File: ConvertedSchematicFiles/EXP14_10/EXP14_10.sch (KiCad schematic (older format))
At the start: 14 parts, among them U1 uA741

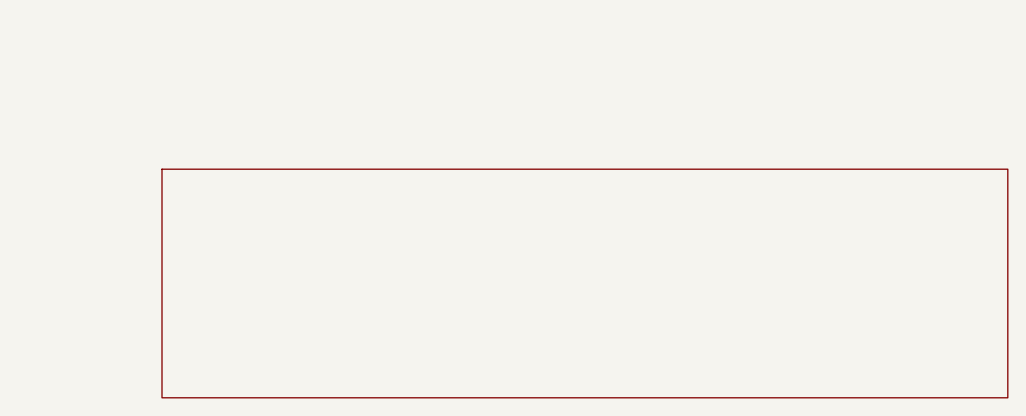
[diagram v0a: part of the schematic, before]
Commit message: Excluded some components. These no longer appear after conversion. When calling shell commands, filenames are in "quotes"
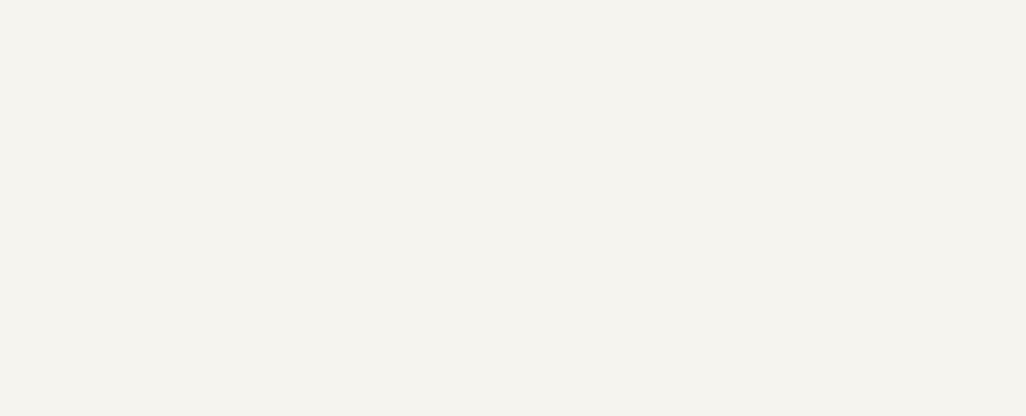
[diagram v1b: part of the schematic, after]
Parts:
- removed titleblk: titleblk, symbol TITLEBLK_PSPICE
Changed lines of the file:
@@
 	0    -1    1    0
-$EndComp
-$Comp
-L TITLEBLK_PSPICE titleblk
-U 1 1 32520059
-P 9700 7200
-F 0 "titleblk" H 19400 14400 30  0001 L CNN
-F 1 "titleblk" H 19400 14480 30  0001 L CNN
-	1    9700 7200
-	1    0    0    1
 $EndComp
 Wire Wire Line

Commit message: Ports issue fixed. Now annotation for ports is #PWR? function added "itos"
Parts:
- removed EGND: EGND, symbol EGND_PSPICE
- removed GND_EARTH (x4): GND_EARTH, symbol GND_EARTH_PSPICE
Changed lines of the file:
@@
 $EndDescr
 $Comp
-L GND_EARTH_PSPICE GND_EARTH
+L GND_EARTH_PSPICE #PWR1
 U 1 1 14289383
 P 2500 3400
-F 0 "GND_EARTH" H 5000 6800 30  0001 L CNN
+F 0 "#PWR1" H 5000 6800 30  0001 L CNN
 F 1 "GND_EARTH" H 5000 6880 30  0001 L CNN
 	1    2500 3400
@@
 $EndComp
 $Comp
-L GND_EARTH_PSPICE GND_EARTH
+L GND_EARTH_PSPICE #PWR2
 U 1 1 46930886
 P 2200 4600
-F 0 "GND_EARTH" H 4400 9200 30  0001 L CNN
+F 0 "#PWR2" H 4400 9200 30  0001 L CNN
 F 1 "GND_EARTH" H 4400 9280 30  0001 L CNN
 	1    2200 4600
@@
 $EndComp
 $Comp
-L GND_EARTH_PSPICE GND_EARTH
+L GND_EARTH_PSPICE #PWR3
 U 1 1 71692777
 P 1400 3700
-F 0 "GND_EARTH" H 2800 7400 30  0001 L CNN
+F 0 "#PWR3" H 2800 7400 30  0001 L CNN
 F 1 "GND_EARTH" H 2800 7480 30  0001 L CNN
 	1    1400 3700
@@
 $EndComp
 $Comp
-L GND_EARTH_PSPICE GND_EARTH
+L GND_EARTH_PSPICE #PWR4
 U 1 1 14636915
 P 900 4500
-F 0 "GND_EARTH" H 1800 9000 30  0001 L CNN
+F 0 "#PWR4" H 1800 9000 30  0001 L CNN
 F 1 "GND_EARTH" H 1800 9080 30  0001 L CNN
 	1    900 4500
@@
 $EndComp
 $Comp
-L EGND_PSPICE EGND
+L EGND_PSPICE #PWR5
 U 1 1 77747793
 P 3100 4400
-F 0 "EGND" H 6200 8800 30  0001 L CNN
+F 0 "#PWR5" H 6200 8800 30  0001 L CNN
 F 1 "EGND" H 6200 8880 30  0001 L CNN
 	1    3100 4400

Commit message: Added LICENSE.txt
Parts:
- VIN: value VAC -> AC
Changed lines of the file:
@@
 $EndDescr
 $Comp
-L GND_EARTH_PSPICE #PWR1
+L GND #PWR1
 U 1 1 14289383
 P 2500 3400
@@
 $EndComp
 $Comp
-L GND_EARTH_PSPICE #PWR2
+L GND #PWR2
 U 1 1 46930886
 P 2200 4600
@@
 $EndComp
 $Comp
-L GND_EARTH_PSPICE #PWR3
+L GND #PWR3
 U 1 1 71692777
 P 1400 3700
@@
 $EndComp
 $Comp
-L GND_EARTH_PSPICE #PWR4
+L GND #PWR4
 U 1 1 14636915
 P 900 4500
@@
 $EndComp
 $Comp
-L EGND_PSPICE #PWR5
+L GND #PWR5
 U 1 1 77747793
 P 3100 4400
@@
 P 900 4100
 F 0 "VIN" H 900 4100 30  0000 L CNN
-F 1 "VAC" H 900 4180 30  0000 L CNN
+F 1 "AC" H 900 4180 30  0000 L CNN
 	1    900 4100
 	1    0    0    1

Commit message: Orientation fix. Library components are now inverted, with +ve y axis going up. In Schematic files, +ve y axis is downwards. This is how the KiCad libraries are. As a result of the above fixed, the converted GND is now oriented correctly.
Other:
- moved on the sheet: VIN
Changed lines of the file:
@@
 F 1 "GND_EARTH" H 5000 6880 30  0001 L CNN
 	1    2500 3400
-	1    0    0    1
+	1    0    0    -1
 $EndComp
 $Comp
@@
 F 1 "GND_EARTH" H 4400 9280 30  0001 L CNN
 	1    2200 4600
-	1    0    0    1
+	1    0    0    -1
 $EndComp
 $Comp
@@
 F 1 "GND_EARTH" H 2800 7480 30  0001 L CNN
 	1    1400 3700
-	1    0    0    1
+	1    0    0    -1
 $EndComp
 $Comp
@@
 F 1 "GND_EARTH" H 1800 9080 30  0001 L CNN
 	1    900 4500
-	1    0    0    1
+	1    0    0    -1
 $EndComp
 $Comp
@@
 F 1 "EGND" H 6200 8880 30  0001 L CNN
 	1    3100 4400
-	1    0    0    1
+	1    0    0    -1
 $EndComp
 $Comp
@@
 F 1 "15v" H 2200 3870 30  0000 C CNN
 	1    2200 3600
-	-1    0    0    -1
+	-1    0    0    1
 $EndComp
 $Comp
@@
 F 1 "15v" H 2200 4490 30  0000 C CNN
 	1    2200 4600
-	-1    0    0    -1
+	-1    0    0    1
 $EndComp
 $Comp
@@
 F 1 "R" H 1400 3780 30  0001 L CNN
 	1    1400 3700
-	1    0    0    1
+	1    0    0    -1
 $EndComp
 $Comp
@@
 F 1 "10k" H 2400 4950 30  0000 L CNN
 	1    2400 4800
-	1    0    0    1
+	1    0    0    -1
 $EndComp
 $Comp
@@
 F 1 "uA741" H 1800 3780 30  0001 L CNN
 	1    1800 3700
-	1    0    0    1
+	1    0    0    -1
 $EndComp
 $Comp
@@
 F 1 "R" H 1100 4180 30  0001 L CNN
 	1    1100 4100
-	1    0    0    1
+	1    0    0    -1
 $EndComp
 $Comp
@@
 F 1 "AC" H 900 4180 30  0000 L CNN
 	1    900 4100
-	1    0    0    1
+	1    0    0    -1
 $EndComp
 $Comp
@@
 F 1 "10k" H 3100 4330 30  0000 L CNN
 	1    3100 4000
-	0    -1    1    0
+	0    1    1    0
 $EndComp
 Wire Wire Line

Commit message: Removed the use of exec, wrote basename function, made integration with eSim easier.
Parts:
- added titleblk: titleblk, symbol titleblk_PSPICE
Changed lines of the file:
@@
-EESchema Schematic File Version 2  date Monday 21 June 1999 09:05:10 PM IST
+EESchema Schematic File Version 2  date
 LIBS:power
 LIBS:device
@@
 LIBS:contrib
 LIBS:valves
-LIBS:ConvertedSchematicFiles/EXP14_10-cache
 EELAYER 25  0
 EELAYER END
@@
 Sheet 1 1
 Title ""
-Date "21 Jun 1999"
+Date ""
 Rev ""
 Comp ""
@@
 	0    1    1    0
 $EndComp
+$Comp
+L titleblk_PSPICE titleblk
+U 1 1 32520059
+P 9700 7200
+F 0 "titleblk" H 19400 14400 30  0001 L CNN
+F 1 "titleblk" H 19400 14480 30  0001 L CNN
+	1    9700 7200
+	1    0    0    -1
+$EndComp
 Wire Wire Line
